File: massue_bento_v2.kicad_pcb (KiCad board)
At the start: 2 copper layers, 100 x 21 mm, 71 parts, among them K1 CONN_3, K2 CONN_3, K3 CONN_3, P1 TST, P10 CONN_1, P11 TST, P12 TST, P13 TST, P14 TST, P15 TST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

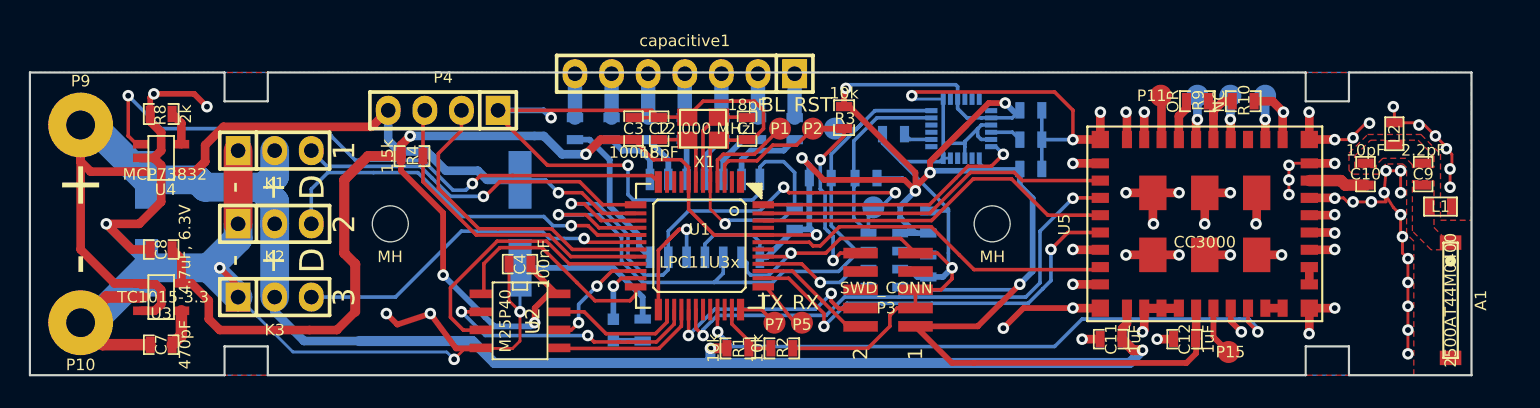
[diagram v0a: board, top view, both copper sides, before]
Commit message: Clean: same value for 100nF/0.1uf capacitors, re-organization of labels, add dimension labels
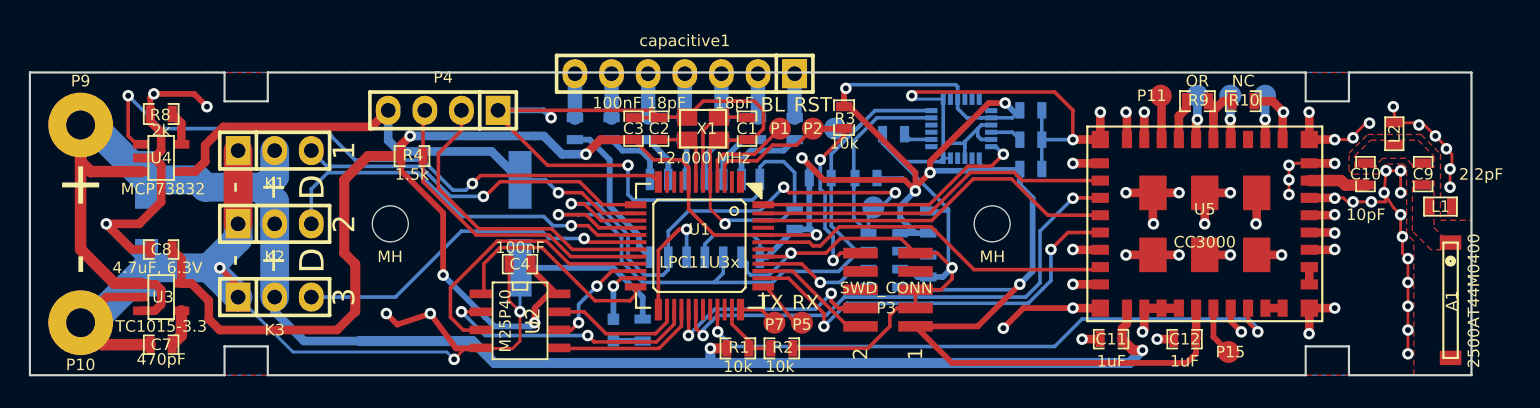
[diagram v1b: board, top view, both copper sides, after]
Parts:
- C15, C17: value 0.1uF -> 100nF
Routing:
- net +5V_USB: track 40.5 -> 41.4 mm
